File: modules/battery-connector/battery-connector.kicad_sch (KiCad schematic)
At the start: 2 parts, among them J1 691210910002

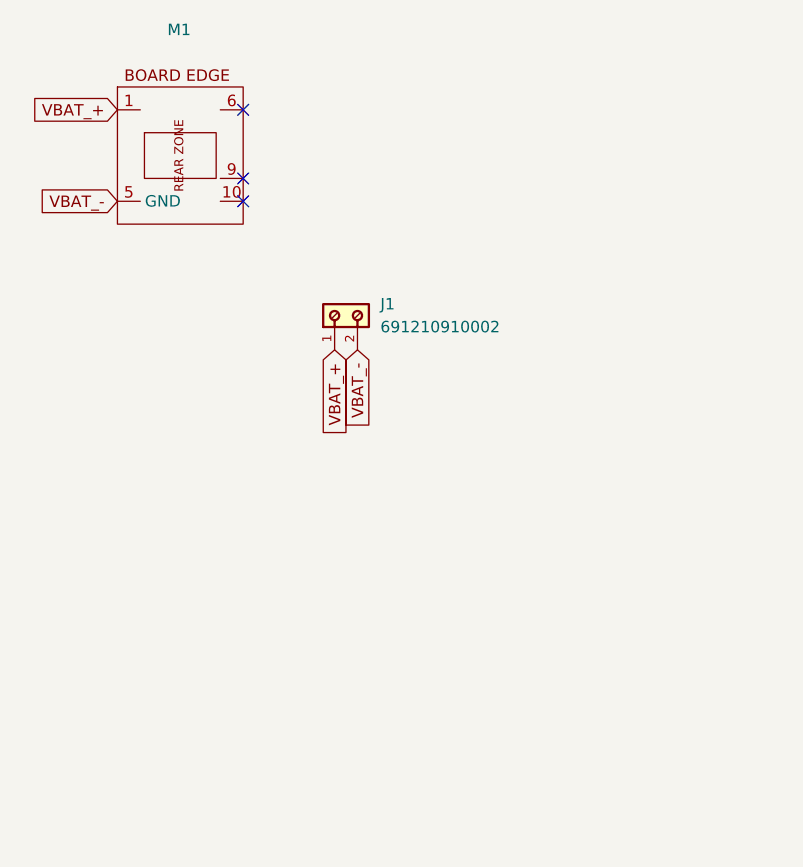
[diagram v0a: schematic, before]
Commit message: Updating workflow to detect kicad changes
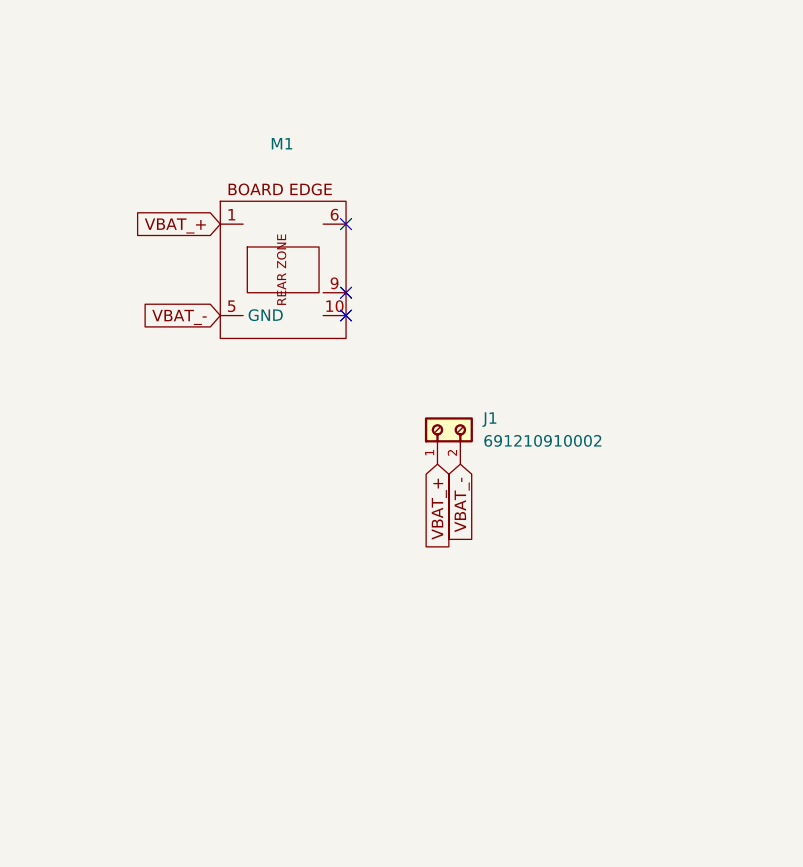
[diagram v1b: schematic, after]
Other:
- moved on the sheet: J1, M1
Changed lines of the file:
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@@
 	(paper "A4")
 	(no_connect
-		(at 107.95 46.99)
+		(at 119.38 59.69)
 	)
 	(no_connect
-		(at 107.95 39.37)
+		(at 119.38 52.07)
 	)
 	(no_connect
-		(at 107.95 49.53)
+		(at 119.38 62.23)
 	)
 	(global_label "VBAT_+"
 		(shape input)
-		(at 93.98 39.37 180)
+		(at 105.41 52.07 180)
 		(fields_autoplaced yes)
 		(effects
@@
 		)
 		(property "Intersheetrefs" "${INTERSHEET_REFS}"
-			(at 84.04 39.37 0)
+			(at 95.47 52.07 0)
 			(effects
 				(font
@@
 	(global_label "VBAT_-"
 		(shape input)
-		(at 93.98 49.53 180)
+		(at 105.41 62.23 180)
 		(fields_autoplaced yes)
 		(effects
@@
 		)
 		(property "Intersheetrefs" "${INTERSHEET_REFS}"
-			(at 84.04 49.53 0)
+			(at 95.47 62.23 0)
 			(effects
 				(font
@@
 	(global_label "VBAT_-"
 		(shape input)
-		(at 120.65 66.04 270)
+		(at 132.08 78.74 270)
 		(fields_autoplaced yes)
 		(effects
@@
 		)
 		(property "Intersheetrefs" "${INTERSHEET_REFS}"
-			(at 120.65 75.98 90)
+			(at 132.08 88.68 90)
 			(effects
 				(font
@@
 	(global_label "VBAT_+"
 		(shape input)
-		(at 118.11 66.04 270)
+		(at 129.54 78.74 270)
 		(fields_autoplaced yes)
 		(effects
@@
 		)
 		(property "Intersheetrefs" "${INTERSHEET_REFS}"
-			(at 118.11 75.98 90)
+			(at 129.54 88.68 90)
 			(effects
 				(font
@@
 	(symbol
 		(lib_id "MegaCastle:MegaCastle2x5-Module-I7.0x7.9-M8CC-EDGE")
-		(at 100.33 44.45 0)
+		(at 111.76 57.15 0)
 		(unit 1)
 		(exclude_from_sim no)
@@
 		(fields_autoplaced yes)
 		(property "Reference" "M1"
-			(at 100.8338 30.48 0)
+			(at 112.2638 43.18 0)
 			(effects
 				(font
@@
 		)
 		(property "Value" "~"
-			(at 100.8338 33.02 0)
+			(at 112.2638 45.72 0)
 			(effects
 				(font
@@
 		)
 		(property "Footprint" "MegaCastle:MegaCastle2x5-Module-I15.0x7.9-M8CC-SPAREPAD"
-			(at 100.33 57.15 0)
+			(at 111.76 69.85 0)
 			(effects
 				(font
@@
 		)
 		(property "Datasheet" ""
-			(at 100.33 39.37 0)
+			(at 111.76 52.07 0)
 			(effects
 				(font
@@
 		)
 		(property "Description" "Generated using footprint-gen .. 7 8 5 M8CC"
-			(at 100.33 44.45 0)
+			(at 111.76 57.15 0)
 			(effects
 				(font
@@
 	(symbol
 		(lib_id "691210910002:691210910002")
-		(at 120.65 60.96 0)
+		(at 132.08 73.66 0)
 		(unit 1)
 		(exclude_from_sim no)
@@
 		(fields_autoplaced yes)
 		(property "Reference" "J1"
-			(at 123.19 60.9599 0)
+			(at 134.62 73.6599 0)
 			(effects
 				(font
@@
 		)
 		(property "Value" "691210910002"
-			(at 123.19 63.4999 0)
+			(at 134.62 76.1999 0)
 			(effects
 				(font
@@
 		)
 		(property "Footprint" "MegaCastle:691210910002"
-			(at 120.65 60.96 0)
+			(at 132.08 73.66 0)
 			(effects
 				(font
@@
 		)
 		(property "Datasheet" ""
-			(at 120.65 60.96 0)
+			(at 132.08 73.66 0)
 			(effects
 				(font
@@
 		)
 		(property "Description" ""
-			(at 120.65 60.96 0)
+			(at 132.08 73.66 0)
 			(effects
 				(font
@@
 		)
 		(property "WIRE" "30 to 18 (AWG) 0.0509 to 0.823 (mm²)"
-			(at 120.65 60.96 0)
+			(at 132.08 73.66 0)
 			(effects
 				(font
@@
 		)
 		(property "MOUNT" "THT"
-			(at 120.65 60.96 0)
+			(at 132.08 73.66 0)
 			(effects
 				(font
@@
 		)
 		(property "IR-UL" "6A"
-			(at 120.65 60.96 0)
+			(at 132.08 73.66 0)
 			(effects
 				(font
@@
 		)
 		(property "WORKING-VOLTAGE-UL" "150V (AC)"
-			(at 120.65 60.96 0)
+			(at 132.08 73.66 0)
 			(effects
 				(font
@@
 		)
 		(property "PART-NUMBER" "691210910002"
-			(at 120.65 60.96 0)
+			(at 132.08 73.66 0)
 			(effects
 				(font
@@
 		)
 		(property "DATASHEET-URL" "https://www.we-online.com/redexpert/spec/691210910002?ae"
-			(at 120.65 60.96 0)
+			(at 132.08 73.66 0)
 			(effects
 				(font
@@
 		)
 		(property "PITCH" "2.54mm"
-			(at 120.65 60.96 0)
+			(at 132.08 73.66 0)
 			(effects
 				(font
@@
 		)
 		(property "PINS" "2"
-			(at 120.65 60.96 0)
+			(at 132.08 73.66 0)
 			(effects
 				(font
@@
 		)
 		(property "TYPE" "Horizontal"
-			(at 120.65 60.96 0)
-			(effects
-				(font
+			(at 132.08 73.66 0)
+			(effects
+				(font

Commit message: Updating all modules
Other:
- moved on the sheet: J1, M1
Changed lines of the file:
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@@
 	(paper "A4")
 	(no_connect
-		(at 119.38 59.69)
+		(at 137.16 91.44)
 	)
 	(no_connect
-		(at 119.38 52.07)
+		(at 137.16 83.82)
 	)
 	(no_connect
-		(at 119.38 62.23)
+		(at 137.16 93.98)
 	)
 	(global_label "VBAT_+"
 		(shape input)
-		(at 105.41 52.07 180)
+		(at 123.19 83.82 180)
 		(fields_autoplaced yes)
 		(effects
@@
 		)
 		(property "Intersheetrefs" "${INTERSHEET_REFS}"
-			(at 95.47 52.07 0)
+			(at 113.25 83.82 0)
 			(effects
 				(font
@@
 	(global_label "VBAT_-"
 		(shape input)
-		(at 105.41 62.23 180)
+		(at 123.19 93.98 180)
 		(fields_autoplaced yes)
 		(effects
@@
 		)
 		(property "Intersheetrefs" "${INTERSHEET_REFS}"
-			(at 95.47 62.23 0)
+			(at 113.25 93.98 0)
 			(effects
 				(font
@@
 	(global_label "VBAT_-"
 		(shape input)
-		(at 132.08 78.74 270)
+		(at 149.86 110.49 270)
 		(fields_autoplaced yes)
 		(effects
@@
 		)
 		(property "Intersheetrefs" "${INTERSHEET_REFS}"
-			(at 132.08 88.68 90)
+			(at 149.86 120.43 90)
 			(effects
 				(font
@@
 	(global_label "VBAT_+"
 		(shape input)
-		(at 129.54 78.74 270)
+		(at 147.32 110.49 270)
 		(fields_autoplaced yes)
 		(effects
@@
 		)
 		(property "Intersheetrefs" "${INTERSHEET_REFS}"
-			(at 129.54 88.68 90)
+			(at 147.32 120.43 90)
 			(effects
 				(font
@@
 	(symbol
 		(lib_id "MegaCastle:MegaCastle2x5-Module-I7.0x7.9-M8CC-EDGE")
-		(at 111.76 57.15 0)
+		(at 129.54 88.9 0)
 		(unit 1)
 		(exclude_from_sim no)
@@
 		(fields_autoplaced yes)
 		(property "Reference" "M1"
-			(at 112.2638 43.18 0)
+			(at 130.0438 74.93 0)
 			(effects
 				(font
@@
 		)
 		(property "Value" "~"
-			(at 112.2638 45.72 0)
+			(at 130.0438 77.47 0)
 			(effects
 				(font
@@
 		)
 		(property "Footprint" "MegaCastle:MegaCastle2x5-Module-I15.0x7.9-M8CC-SPAREPAD"
-			(at 111.76 69.85 0)
+			(at 129.54 101.6 0)
 			(effects
 				(font
@@
 		)
 		(property "Datasheet" ""
-			(at 111.76 52.07 0)
+			(at 129.54 83.82 0)
 			(effects
 				(font
@@
 		)
 		(property "Description" "Generated using footprint-gen .. 7 8 5 M8CC"
-			(at 111.76 57.15 0)
+			(at 129.54 88.9 0)
 			(effects
 				(font
@@
 	(symbol
 		(lib_id "691210910002:691210910002")
-		(at 132.08 73.66 0)
+		(at 149.86 105.41 0)
 		(unit 1)
 		(exclude_from_sim no)
@@
 		(fields_autoplaced yes)
 		(property "Reference" "J1"
-			(at 134.62 73.6599 0)
+			(at 152.4 105.4099 0)
 			(effects
 				(font
@@
 		)
 		(property "Value" "691210910002"
-			(at 134.62 76.1999 0)
+			(at 152.4 107.9499 0)
 			(effects
 				(font
@@
 		)
 		(property "Footprint" "MegaCastle:691210910002"
-			(at 132.08 73.66 0)
+			(at 149.86 105.41 0)
 			(effects
 				(font
@@
 		)
 		(property "Datasheet" ""
-			(at 132.08 73.66 0)
+			(at 149.86 105.41 0)
 			(effects
 				(font
@@
 		)
 		(property "Description" ""
-			(at 132.08 73.66 0)
+			(at 149.86 105.41 0)
 			(effects
 				(font
@@
 		)
 		(property "WIRE" "30 to 18 (AWG) 0.0509 to 0.823 (mm²)"
-			(at 132.08 73.66 0)
+			(at 149.86 105.41 0)
 			(effects
 				(font
@@
 		)
 		(property "MOUNT" "THT"
-			(at 132.08 73.66 0)
+			(at 149.86 105.41 0)
 			(effects
 				(font
@@
 		)
 		(property "IR-UL" "6A"
-			(at 132.08 73.66 0)
+			(at 149.86 105.41 0)
 			(effects
 				(font
@@
 		)
 		(property "WORKING-VOLTAGE-UL" "150V (AC)"
-			(at 132.08 73.66 0)
+			(at 149.86 105.41 0)
 			(effects
 				(font
@@
 		)
 		(property "PART-NUMBER" "691210910002"
-			(at 132.08 73.66 0)
+			(at 149.86 105.41 0)
 			(effects
 				(font
@@
 		)
 		(property "DATASHEET-URL" "https://www.we-online.com/redexpert/spec/691210910002?ae"
-			(at 132.08 73.66 0)
+			(at 149.86 105.41 0)
 			(effects
 				(font
@@
 		)
 		(property "PITCH" "2.54mm"
-			(at 132.08 73.66 0)
+			(at 149.86 105.41 0)
 			(effects
 				(font
@@
 		)
 		(property "PINS" "2"
-			(at 132.08 73.66 0)
+			(at 149.86 105.41 0)
 			(effects
 				(font
@@
 		)
 		(property "TYPE" "Horizontal"
-			(at 132.08 73.66 0)
-			(effects
-				(font
+			(at 149.86 105.41 0)
+			(effects
+				(font
